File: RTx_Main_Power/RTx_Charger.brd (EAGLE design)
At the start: 102.9 x 75.2 mm, 18 parts, among them IC1 TL331, Q1 STW11NM80

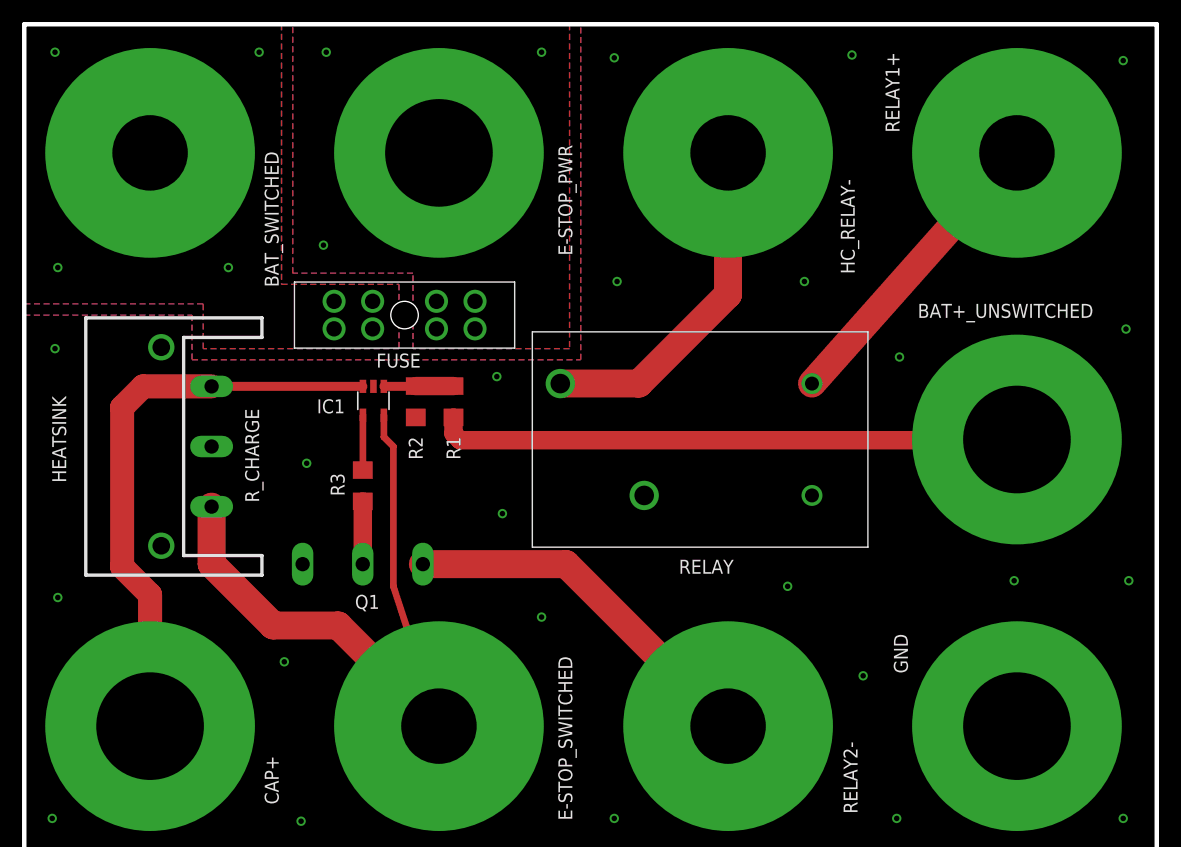
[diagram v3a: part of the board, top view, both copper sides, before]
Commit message: Completed charger board and BOM.
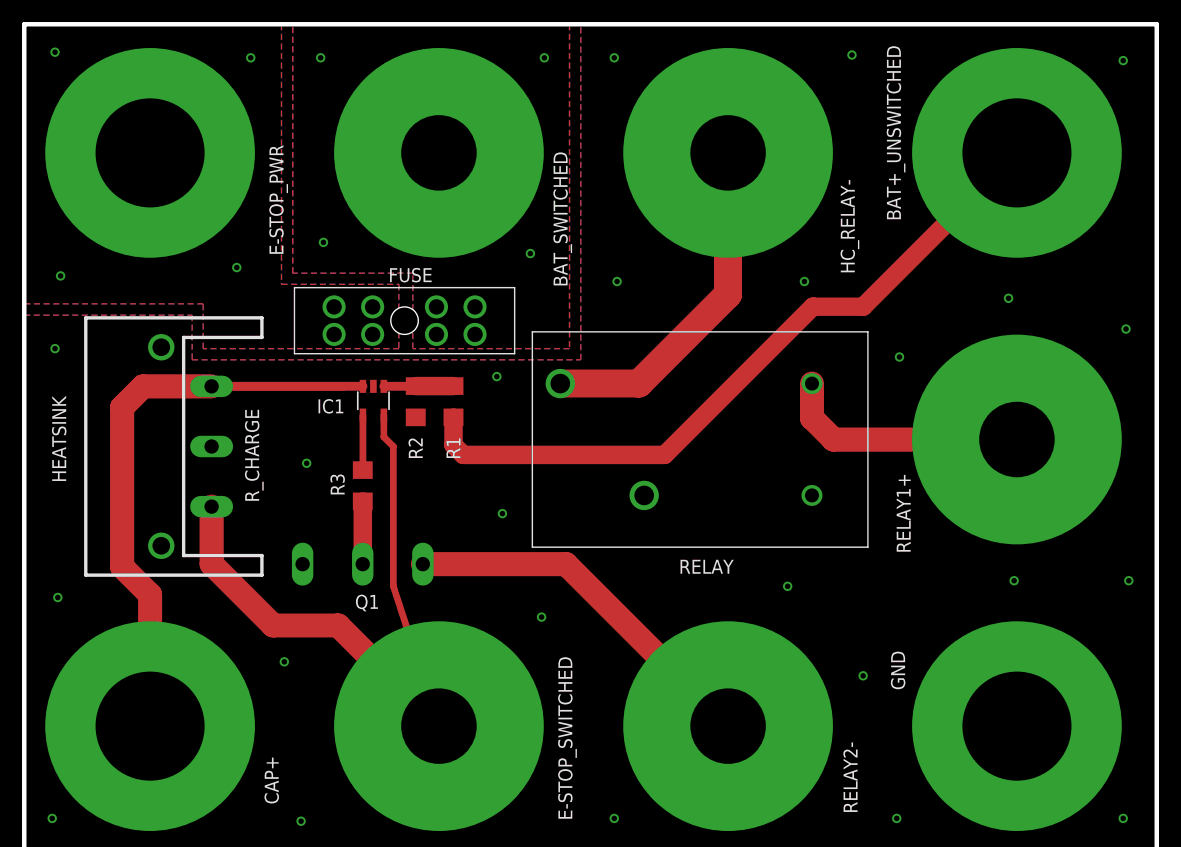
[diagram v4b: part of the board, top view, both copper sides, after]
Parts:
- moved BAT_SWITCHED 26.2 mm to (37.7, 63.5)
- moved E-STOP_PWR 26.2 mm to (11.4, 63.5)
- moved BAT+_UNSWITCHED 26.0 mm to (90.2, 63.5)
- moved RELAY1+ 26.0 mm to (90.2, 37.5)
- moved FUSE 0.51 mm to (34.5, 48.3), turned to 0 degrees
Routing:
- net BAT+_UNSWITCHED: track 52.9 -> 65.4 mm
- net E-STOP_IN: track 28.0 -> 22.6 mm
